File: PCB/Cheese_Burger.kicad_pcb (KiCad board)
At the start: 2 copper layers, 99 x 100 mm, 50 parts, among them J1 BH-14SG, J2 JST_XA_1x2, Q1 2SK4017, Q2 2SK2796, Q3 2SK2796, SW1 SW_SPDT, U1 R-78E3.3-0.5, U2 NJM2742D, U3 NJU7072D, U4 NJU7072D

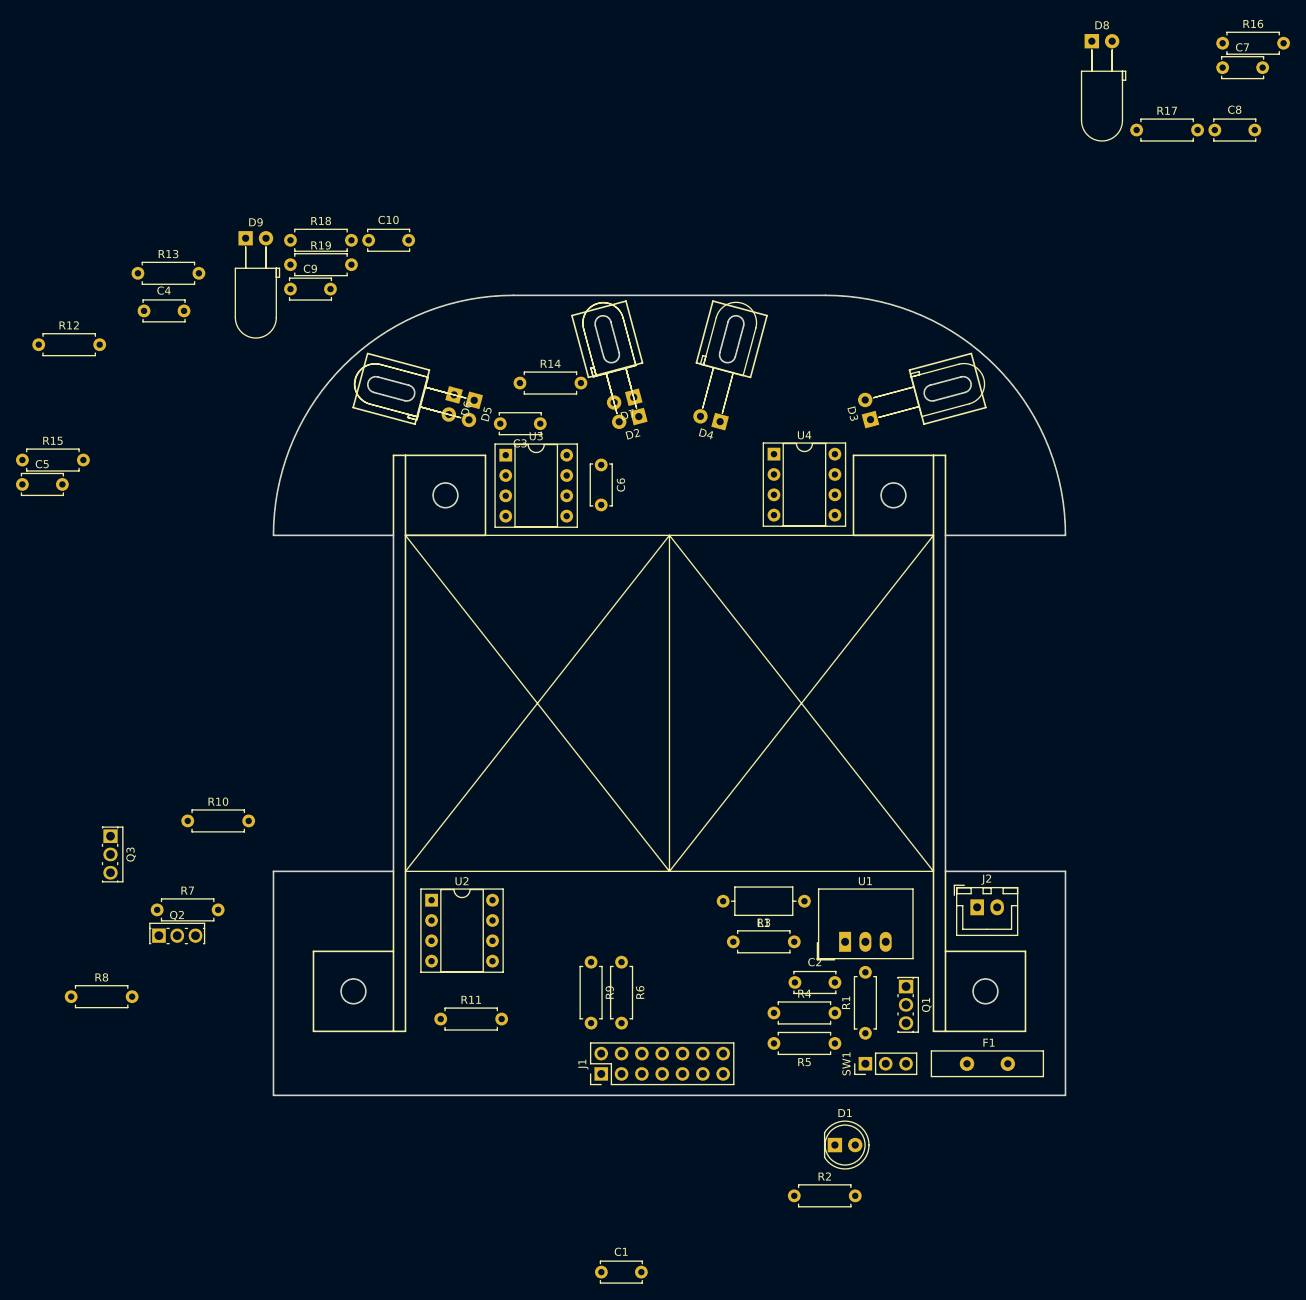
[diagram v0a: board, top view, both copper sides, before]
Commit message: 下側の基板の配線が終了
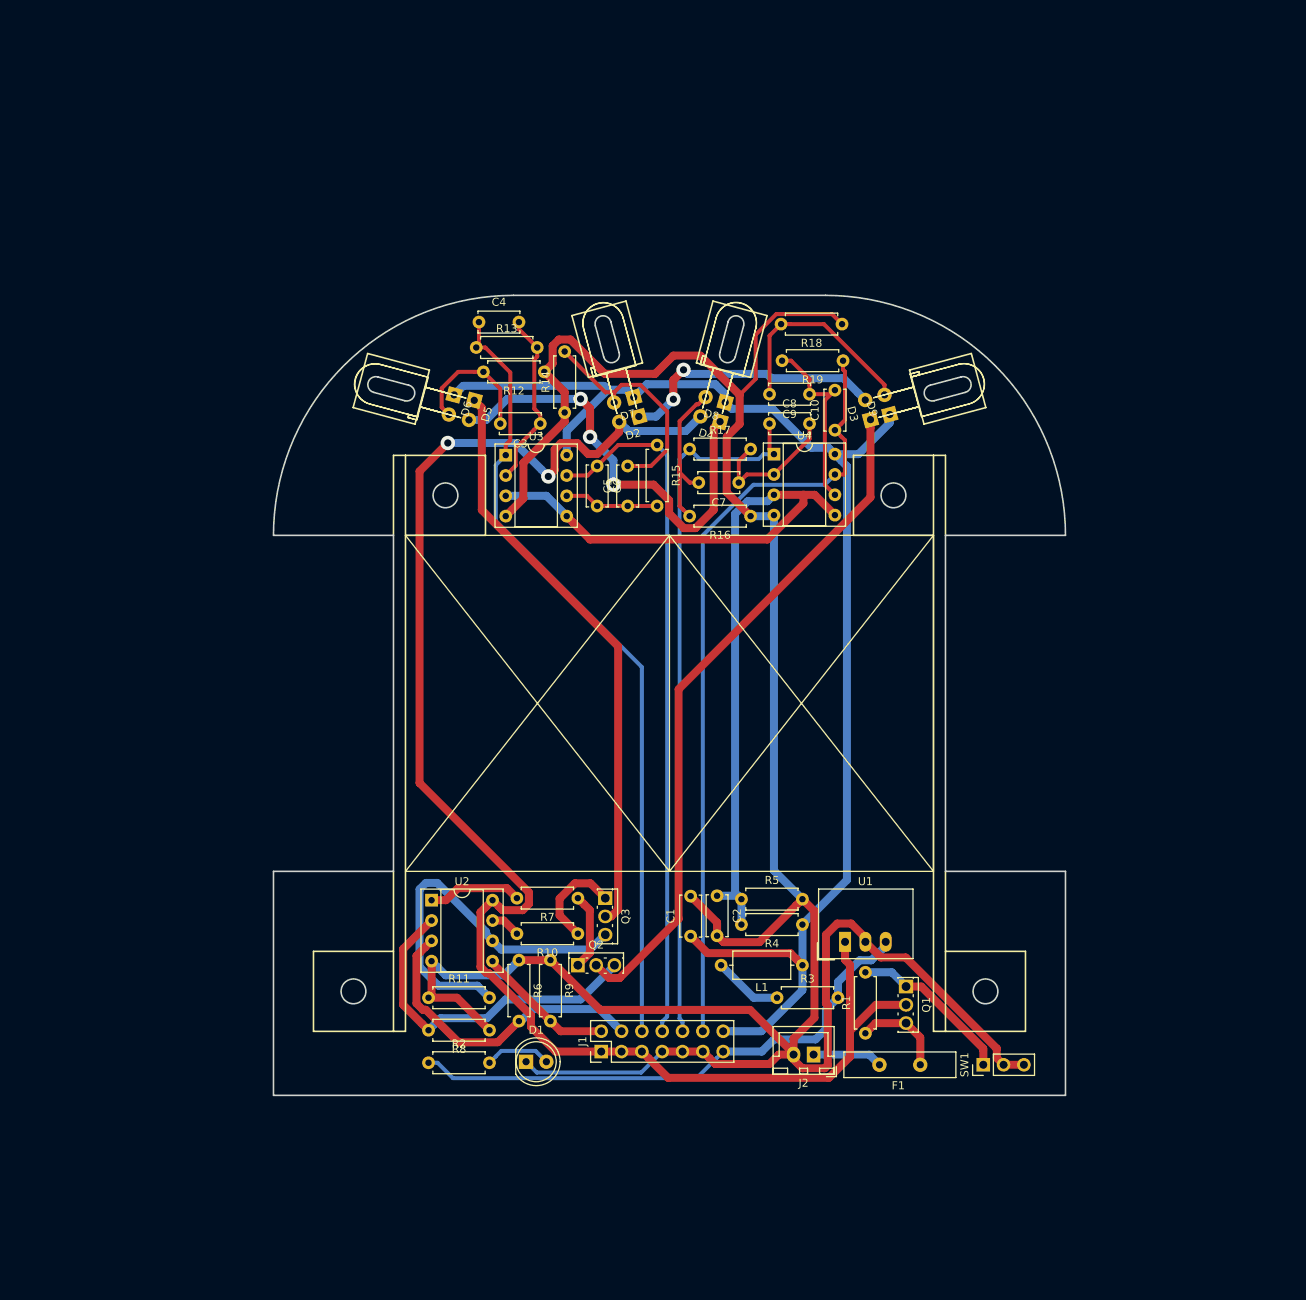
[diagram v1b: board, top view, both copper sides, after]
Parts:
- moved R16 83.5 mm to (159.6, 77.6), turned to 180 degrees
- moved D9 83.5 mm to (177.0, 64.9), turned to 105 degrees
- moved C7 79.7 mm to (158.2, 73.4), turned to 180 degrees
- moved R15 79.4 mm to (148.0, 68.7), turned to 270 degrees
- moved C5 75.7 mm to (144.3, 76.3), turned to 90 degrees
- moved R19 70.1 mm to (171.2, 58.2), turned to 180 degrees
- moved R18 69.7 mm to (171.1, 53.6), turned to 180 degrees
- moved R17 68.6 mm to (152.0, 69.2)
- moved C8 66.7 mm to (162.0, 66.0)
- moved C9 66.2 mm to (167.0, 62.4), turned to 180 degrees
- moved D8 64.3 mm to (156.5, 63.4), turned to 165 degrees
- moved R12 63.3 mm to (133.9, 59.6), turned to 180 degrees
- moved C10 62.9 mm to (170.2, 66.8), turned to 90 degrees
- moved Q3 62.3 mm to (141.5, 125.3)
- moved R7 52.6 mm to (138.0, 125.3), turned to 180 degrees
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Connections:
- SW1 pad 3: (no net) -> GND
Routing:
- net GND: track 0.00 -> 342.8 mm
- net BATT: track 0.00 -> 199.9 mm, vias 0 -> 2
- net 3.3VA: track 0.00 -> 170.8 mm
- net 1.65V: track 0.00 -> 111.8 mm
- net /IR_Sensor1/IR_SENSOR_OUT: track 0.00 -> 99.5 mm
- net /IR_Sensor4/IR_SENSOR_OUT: track 0.00 -> 98.2 mm
- net /IR_Sensor3/IR_SENSOR_OUT: track 0.00 -> 88.8 mm
- net /IR_Sensor2/IR_SENSOR_OUT: track 0.00 -> 86.9 mm
- net Net-(D3-Pad1): track 0.00 -> 86.4 mm
- net Net-(D5-Pad1): track 0.00 -> 73.1 mm
- net 3.3V: track 0.00 -> 67.9 mm
- net Net-(D4-Pad1): track 0.00 -> 55.5 mm, vias 0 -> 3
- net Net-(Q3-Pad3): track 0.00 -> 48.0 mm
- net Net-(Q2-Pad3): track 0.00 -> 43.1 mm
- net /IR_LED2/IR_LED_IN: track 0.00 -> 38.9 mm
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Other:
- net class Elecrow added: clearance 0.2032, trace_width 0.25, via_dia 0.8, via_drill 0.4
